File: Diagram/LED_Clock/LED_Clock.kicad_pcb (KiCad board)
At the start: 2 copper layers, 190.5 x 159.4 mm, 79 parts, among them SW1 SW_Push_Dual, U1 ATmega328P-PU, U2 DS3231MZ, U3 MCP23017-E_SP, U4 MCP23017-E_SP, U5 Barreljack, U6 JST4pin, Y1 Crystal

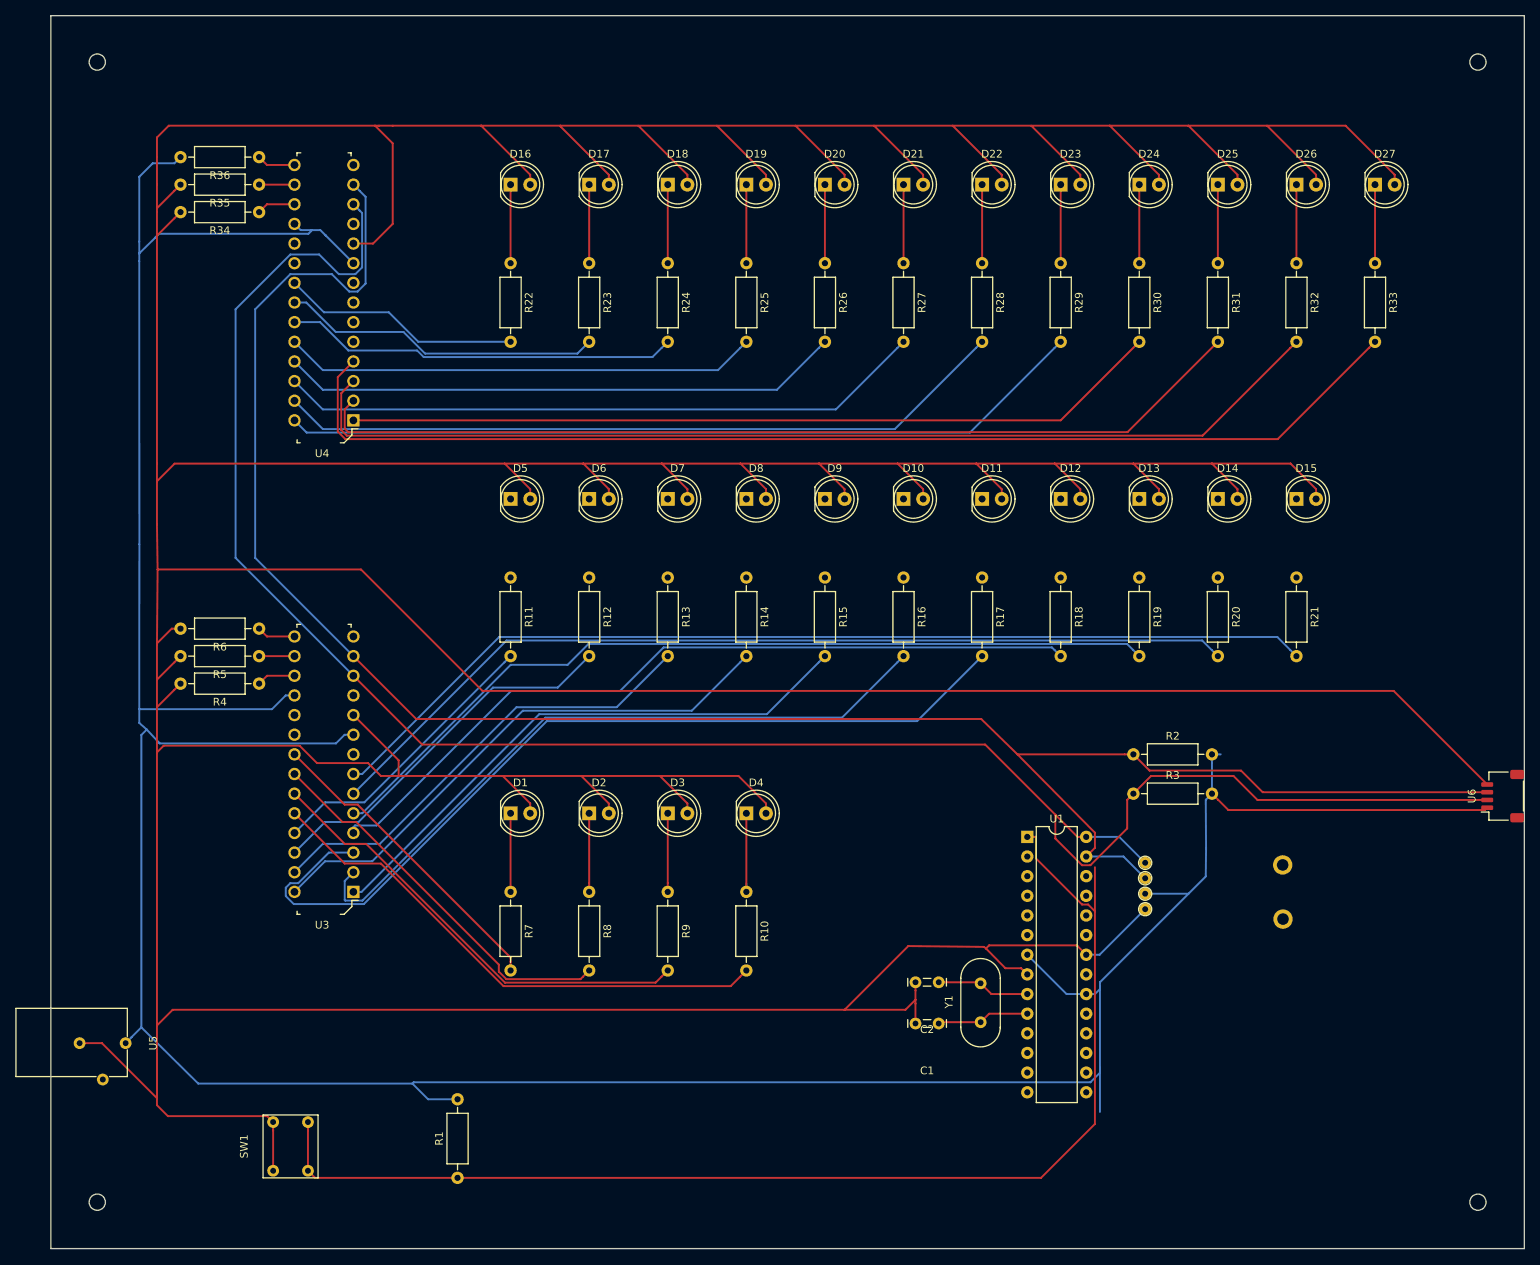
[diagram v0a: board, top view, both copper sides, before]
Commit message: Ground Plane
Added a ground plane and some traces.
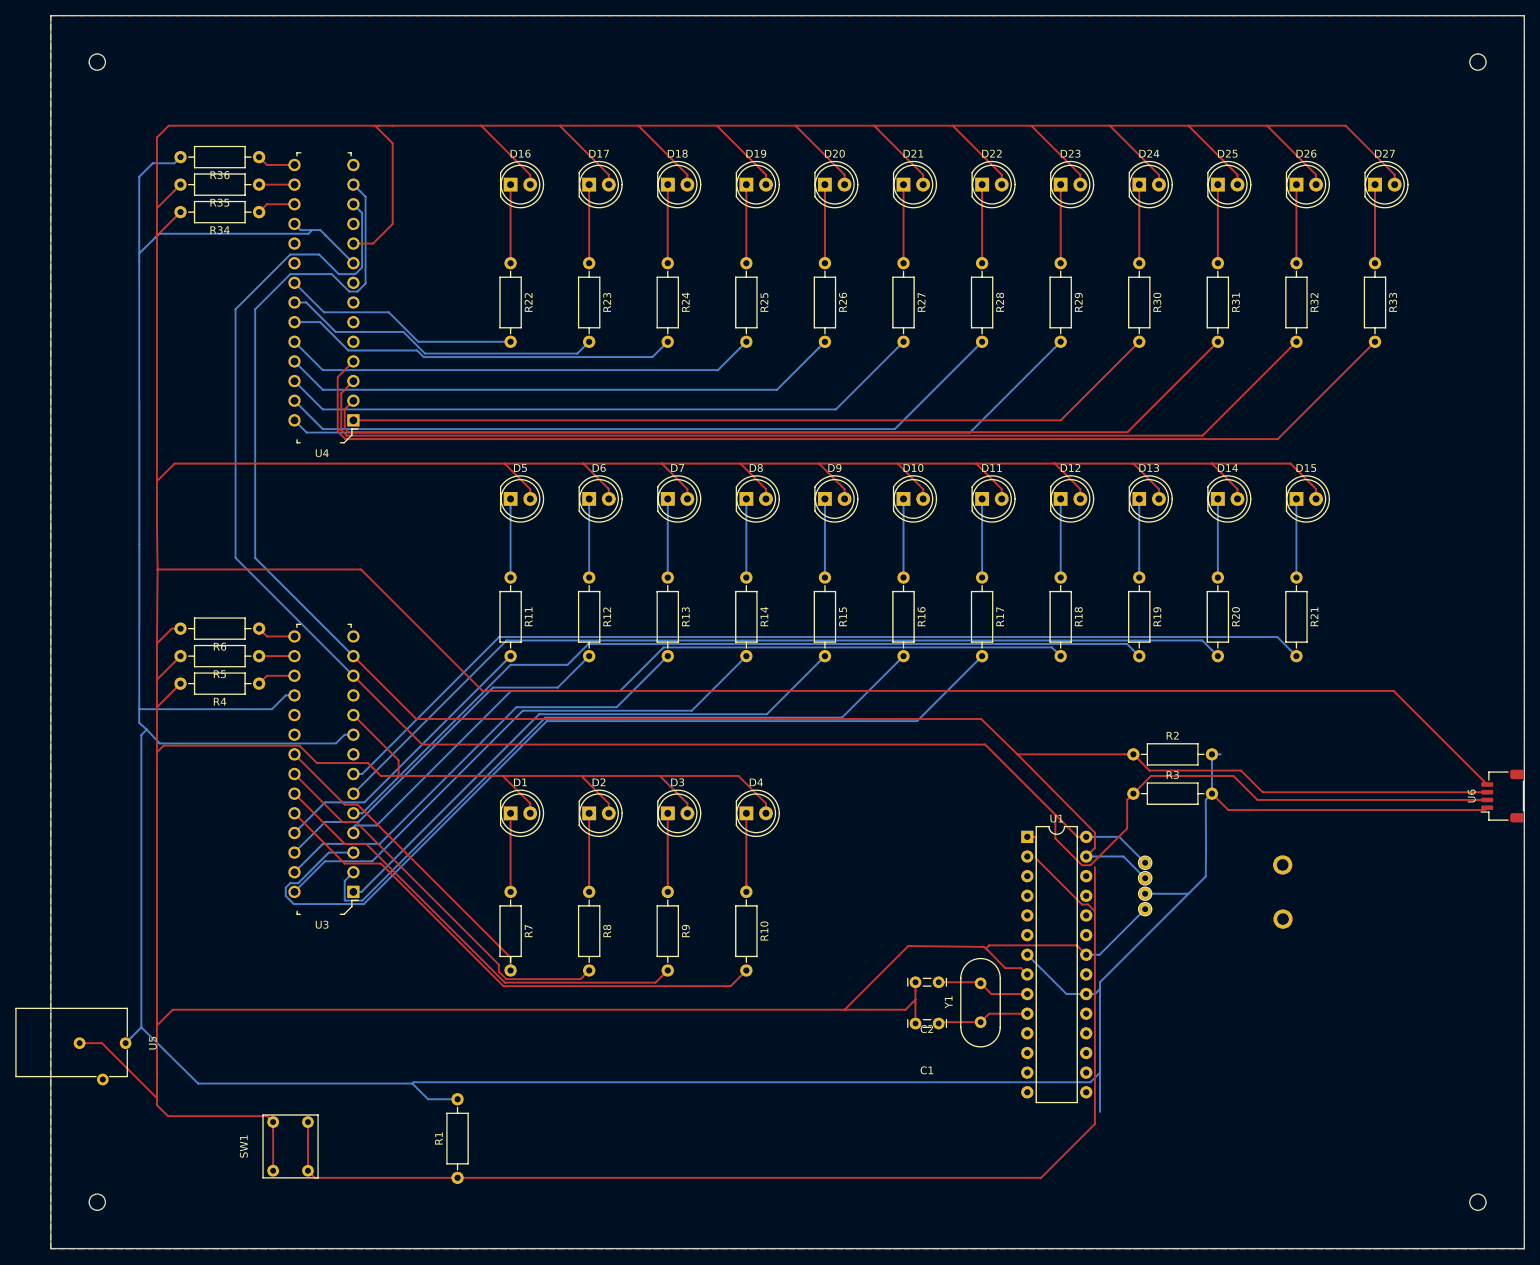
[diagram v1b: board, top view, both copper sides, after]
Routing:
- net Net-(D9-Pad1): track 0.00 -> 10.2 mm
- net Net-(D8-Pad1): track 0.00 -> 10.2 mm
- net Net-(D7-Pad1): track 0.00 -> 10.2 mm
- net Net-(D6-Pad1): track 0.00 -> 10.2 mm
- net Net-(D5-Pad1): track 0.00 -> 10.2 mm
- net Net-(D15-Pad1): track 0.00 -> 10.2 mm
- net Net-(D14-Pad1): track 0.00 -> 10.2 mm
- net Net-(D13-Pad1): track 0.00 -> 10.2 mm
- net Net-(D12-Pad1): track 0.00 -> 10.2 mm
- net Net-(D11-Pad1): track 0.00 -> 10.2 mm
- net Net-(D10-Pad1): track 0.00 -> 10.2 mm
- added copper zone on F.Cu, net GND
